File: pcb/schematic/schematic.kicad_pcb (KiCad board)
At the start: 2 copper layers, 78.5 x 52 mm, 35 parts, among them J1 284391-2, J2 284391-2, J3 284391-2, J4 284391-2, J5 USB_C_Receptacle_USB2.0_16P, K1 G5V-1, Q1 MMBT3904, SW1 BOOT_BTN, SW2 RESET_BTN, U1 ESP32-C3-WROOM-02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

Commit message: update footprint of C4 capacitor to 0805
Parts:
- C4: value 22uF Tantalum -> 22uF; footprint Capacitor_Tantalum_SMD:CP_EIA-3216-18_Kemet-A_HandSolder -> Capacitor_SMD:C_0805_2012Metric
- moved C4 0.56 mm to (127.0, 107.0)
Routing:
- net +3.3V: track 90.6 -> 91.7 mm
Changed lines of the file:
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@@
 		)
 	)
-	(footprint "Capacitor_Tantalum_SMD:CP_EIA-3216-18_Kemet-A_HandSolder"
-		(layer "F.Cu")
-		(at 127.56 107 180)
-		(descr "Tantalum Capacitor SMD Kemet-A (3216-18 Metric), IPC-7352 nominal, (Body size from: http://www.kemet.com/Lists/ProductCatalog/Attachments/253/KEM_TC101_STD.pdf), generated with kicad-footprint-generator")
-		(tags "capacitor tantalum")
-		(property "Reference" "C4"
-			(at 0 -1.75 0)
-			(layer "F.SilkS")
-			(effects
-				(font
-					(size 1 1)
-					(thickness 0.15)
-				)
-			)
-		)
-		(property "Value" "22uF Tantalum"
-			(at 0 1.75 0)
-			(layer "F.Fab")
-			(effects
-				(font
-					(size 1 1)
-					(thickness 0.15)
-				)
-			)
-		)
-		(property "Datasheet" "~"
-			(at 0 0 0)
-			(layer "F.Fab")
-			(hide yes)
-			(effects
-				(font
-					(size 1.27 1.27)
-					(thickness 0.15)
-				)
-			)
-		)
-		(property "Description" "Polarized capacitor"
-			(at 0 0 0)
-			(layer "F.Fab")
-			(hide yes)
-			(effects
-				(font
-					(size 1.27 1.27)
-					(thickness 0.15)
-				)
-			)
-		)
-		(property "LCSC Part #" "C45783"
-			(at 0 0 180)
-			(unlocked yes)
-			(layer "F.Fab")
-			(hide yes)
-			(effects
-				(font
-					(size 1 1)
-					(thickness 0.15)
-				)
-			)
-		)
-		(property ki_fp_filters "CP_*")
-		(sheetname "/")
-		(sheetfile "schematic.kicad_sch")
-		(attr smd)
-		(fp_line
-			(start 1.6 -0.955)
-			(end -2.495 -0.955)
-			(stroke
-				(width 0.12)
-				(type solid)
-			)
-			(layer "F.SilkS")
-		)
-		(fp_line
-			(start -2.495 0.955)
-			(end 1.6 0.955)
-			(stroke
-				(width 0.12)
-				(type solid)
-			)
-			(layer "F.SilkS")
-		)
-		(fp_line
-			(start -2.495 -0.955)
-			(end -2.495 0.955)
-			(stroke
-				(width 0.12)
-				(type solid)
-			)
-			(layer "F.SilkS")
-		)
-		(fp_rect
-			(start -2.49 -1.05)
-			(end 2.49 1.05)
-			(stroke
-				(width 0.05)
-				(type solid)
-			)
-			(fill no)
-			(layer "F.CrtYd")
-		)
-		(fp_line
-			(start 1.6 0.8)
-			(end 1.6 -0.8)
-			(stroke
-				(width 0.1)
-				(type solid)
-			)
-			(layer "F.Fab")
-		)
-		(fp_line
-			(start 1.6 -0.8)
-			(end -1.2 -0.8)
-			(stroke
-				(width 0.1)
-				(type solid)
-			)
-			(layer "F.Fab")
-		)
-		(fp_line
-			(start -1.2 -0.8)
-			(end -1.6 -0.4)
-			(stroke
-				(width 0.1)
-				(type solid)
-			)
-			(layer "F.Fab")
-		)
-		(fp_line
-			(start -1.6 0.8)
-			(end 1.6 0.8)
-			(stroke
-				(width 0.1)
-				(type solid)
-			)
-			(layer "F.Fab")
-		)
-		(fp_line
-			(start -1.6 -0.4)
-			(end -1.6 0.8)
-			(stroke
-				(width 0.1)
-				(type solid)
-			)
-			(layer "F.Fab")
-		)
-		(fp_text user "${REFERENCE}"
-			(at 0 0 0)
-			(layer "F.Fab")
-			(effects
-				(font
-					(size 0.8 0.8)
-					(thickness 0.12)
-				)
-			)
-		)
-		(pad "1" smd roundrect
-			(at -1.44 0 180)
-			(size 1.59 1.39)
-			(layers "F.Cu" "F.Mask" "F.Paste")
-			(roundrect_rratio 0.179856)
-			(net 3 "+3.3V")
-			(pintype "passive")
-		)
-		(pad "2" smd roundrect
-			(at 1.44 0 180)
-			(size 1.59 1.39)
-			(layers "F.Cu" "F.Mask" "F.Paste")
-			(roundrect_rratio 0.179856)
-			(net 1 "GND")
-			(pintype "passive")
-		)
-		(embedded_fonts no)
-		(model "${KICAD9_3DMODEL_DIR}/Capacitor_Tantalum_SMD.3dshapes/CP_EIA-3216-18_Kemet-A.step"
-			(offset
-				(xyz 0 0 0)
-			)
-			(scale
-				(xyz 1 1 1)
-			)
-			(rotate
-				(xyz 0 0 0)
-			)
-		)
-	)
 	(footprint "Capacitor_SMD:C_0805_2012Metric"
 		(layer "F.Cu")
@@
 		)
 	)
+	(footprint "Capacitor_SMD:C_0805_2012Metric"
+		(layer "F.Cu")
+		(at 127 107 180)
+		(descr "Capacitor SMD 0805 (2012 Metric), square (rectangular) end terminal, IPC-7351 nominal, (Body size source: IPC-SM-782 page 76, https://www.pcb-3d.com/wordpress/wp-content/uploads/ipc-sm-782a_amendment_1_and_2.pdf, https://docs.google.com/spreadsheets/d/1BsfQQcO9C6DZCsRaXUlFlo91Tg2WpOkGARC1WS5S8t0/edit?usp=sharing), generated with kicad-footprint-generator")
+		(tags "capacitor")
+		(property "Reference" "C4"
+			(at 0 -1.68 0)
+			(layer "F.SilkS")
+			(effects
+				(font
+					(size 1 1)
+					(thickness 0.15)
+				)
+			)
+		)
+		(property "Value" "22uF"
+			(at 0 1.68 0)
+			(layer "F.Fab")
+			(effects
+				(font
+					(size 1 1)
+					(thickness 0.15)
+				)
+			)
+		)
+		(property "Datasheet" "~"
+			(at 0 0 0)
+			(layer "F.Fab")
+			(hide yes)
+			(effects
+				(font
+					(size 1.27 1.27)
+					(thickness 0.15)
+				)
+			)
+		)
+		(property "Description" "Unpolarized capacitor"
+			(at 0 0 0)
+			(layer "F.Fab")
+			(hide yes)
+			(effects
+				(font
+					(size 1.27 1.27)
+					(thickness 0.15)
+				)
+			)
+		)
+		(property "LCSC Part #" "C45783"
+			(at 0 0 180)
+			(unlocked yes)
+			(layer "F.Fab")
+			(hide yes)
+			(effects
+				(font
+					(size 1 1)
+					(thickness 0.15)
+				)
+			)
+		)
+		(property ki_fp_filters "C_*")
+		(sheetname "/")
+		(sheetfile "schematic.kicad_sch")
+		(attr smd)
+		(fp_line
+			(start -0.261252 0.735)
+			(end 0.261252 0.735)
+			(stroke
+				(width 0.12)
+				(type solid)
+			)
+			(layer "F.SilkS")
+		)
+		(fp_line
+			(start -0.261252 -0.735)
+			(end 0.261252 -0.735)
+			(stroke
+				(width 0.12)
+				(type solid)
+			)
+			(layer "F.SilkS")
+		)
+		(fp_rect
+			(start -1.7 -0.98)
+			(end 1.7 0.98)
+			(stroke
+				(width 0.05)
+				(type solid)
+			)
+			(fill no)
+			(layer "F.CrtYd")
+		)
+		(fp_rect
+			(start -1 -0.625)
+			(end 1 0.625)
+			(stroke
+				(width 0.1)
+				(type solid)
+			)
+			(fill no)
+			(layer "F.Fab")
+		)
+		(fp_text user "${REFERENCE}"
+			(at 0 0 0)
+			(layer "F.Fab")
+			(effects
+				(font
+					(size 0.5 0.5)
+					(thickness 0.08)
+				)
+			)
+		)
+		(pad "1" smd roundrect
+			(at -0.95 0 180)
+			(size 1 1.45)
+			(layers "F.Cu" "F.Mask" "F.Paste")
+			(roundrect_rratio 0.25)
+			(net 3 "+3.3V")
+			(pintype "passive")
+		)
+		(pad "2" smd roundrect
+			(at 0.95 0 180)
+			(size 1 1.45)
+			(layers "F.Cu" "F.Mask" "F.Paste")
+			(roundrect_rratio 0.25)
+			(net 1 "GND")
+			(pintype "passive")
+		)
+		(embedded_fonts no)
+		(model "${KICAD9_3DMODEL_DIR}/Capacitor_SMD.3dshapes/C_0805_2012Metric.step"
+			(offset
+				(xyz 0 0 0)
+			)
+			(scale
+				(xyz 1 1 1)
+			)
+			(rotate
+				(xyz 0 0 0)
+			)
+		)
+	)
 	(footprint "Package_TO_SOT_SMD:SOT-223-3_TabPin2"
 		(layer "F.Cu")
@@
 		(width 0.5)
 		(layer "F.Cu")
+		(net 3)
+	)
+	(segment
+		(start 129 107)
+		(end 127.95 107)
+		(width 0.5)
+		(layer "F.Cu")

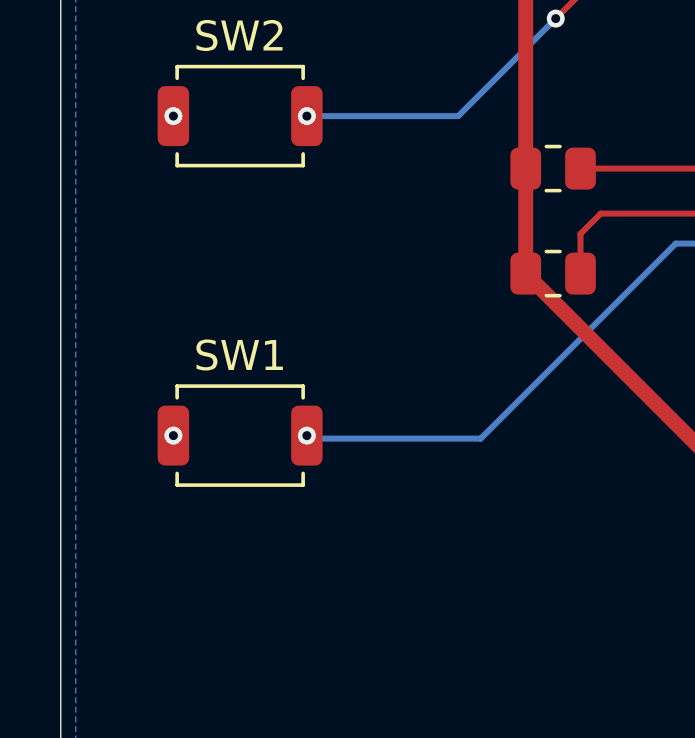
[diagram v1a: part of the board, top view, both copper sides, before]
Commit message: fix silkscreen for boot, reset buttons
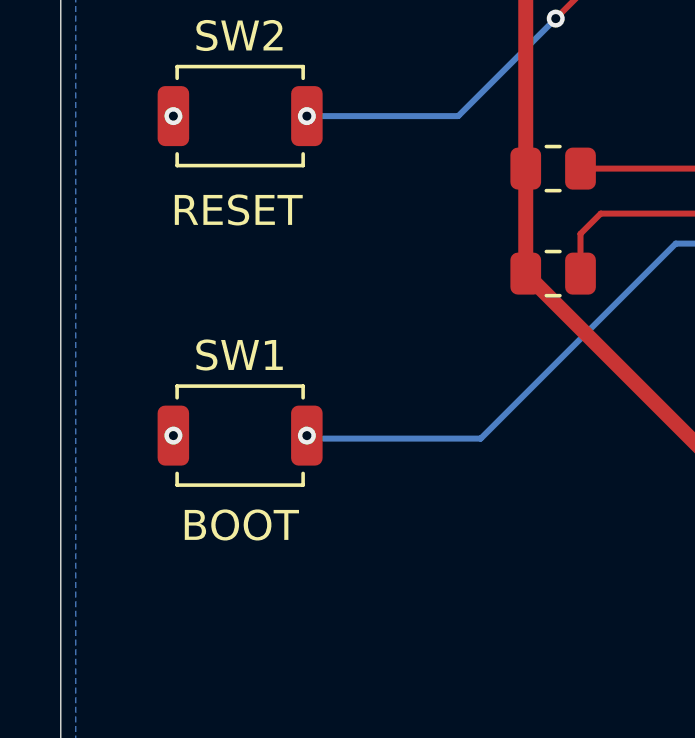
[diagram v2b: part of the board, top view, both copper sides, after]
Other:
- board text added: "BOOT"
- board text added: "RESET"
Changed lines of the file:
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@@
 			(at 0 2.65 0)
 			(layer "F.Fab")
+			(hide yes)
 			(effects
 				(font
@@
 	(footprint "Button_Switch_SMD:SW_SPST_TS-1088-xR025"
 		(layer "F.Cu")
-		(at 107.48 109.4)
+		(at 107.478571 109.4)
 		(descr "SMD Tactile Switch, 3.9x3x2.5 mm, https://lcsc.com/datasheet/lcsc_datasheet_2504101957_XUNPU-TS-1088-AR02016_C720477.pdf")
 		(tags "Tactile Switch")
@@
 			(at 0 2.65 0)
 			(layer "F.Fab")
+			(hide yes)
 			(effects
 				(font
@@
 		(layer "Edge.Cuts")
 	)
+	(gr_text "BOOT"
+		(at 105.5 113 0)
+		(layer "F.SilkS")
+		(effects
+			(font
+				(size 1 1)
+				(thickness 0.1)
+			)
+			(justify left bottom)
+		)
+	)
+	(gr_text "RESET"
+		(at 105.168095 102.5 0)
+		(layer "F.SilkS")
+		(effects
+			(font
+				(size 1 1)
+				(thickness 0.1)
+			)
+			(justify left bottom)
+		)
+	)
 	(gr_text "-5V"
